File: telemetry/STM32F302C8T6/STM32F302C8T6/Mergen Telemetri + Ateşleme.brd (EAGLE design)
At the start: 49.7 x 87.5 mm, 91 parts, among them J2 U.FL, Q2 IRLML6344TRPBF, Q3 IRLML6344TRPBF, U2 BMP280, U3 MPU-6050, U4 L86, U6 AMS1117-3.3, U7 AMS1117-3.3, U8 STM32F302C8T6, X1 JST-XH-04-PIN-LONG-PAD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

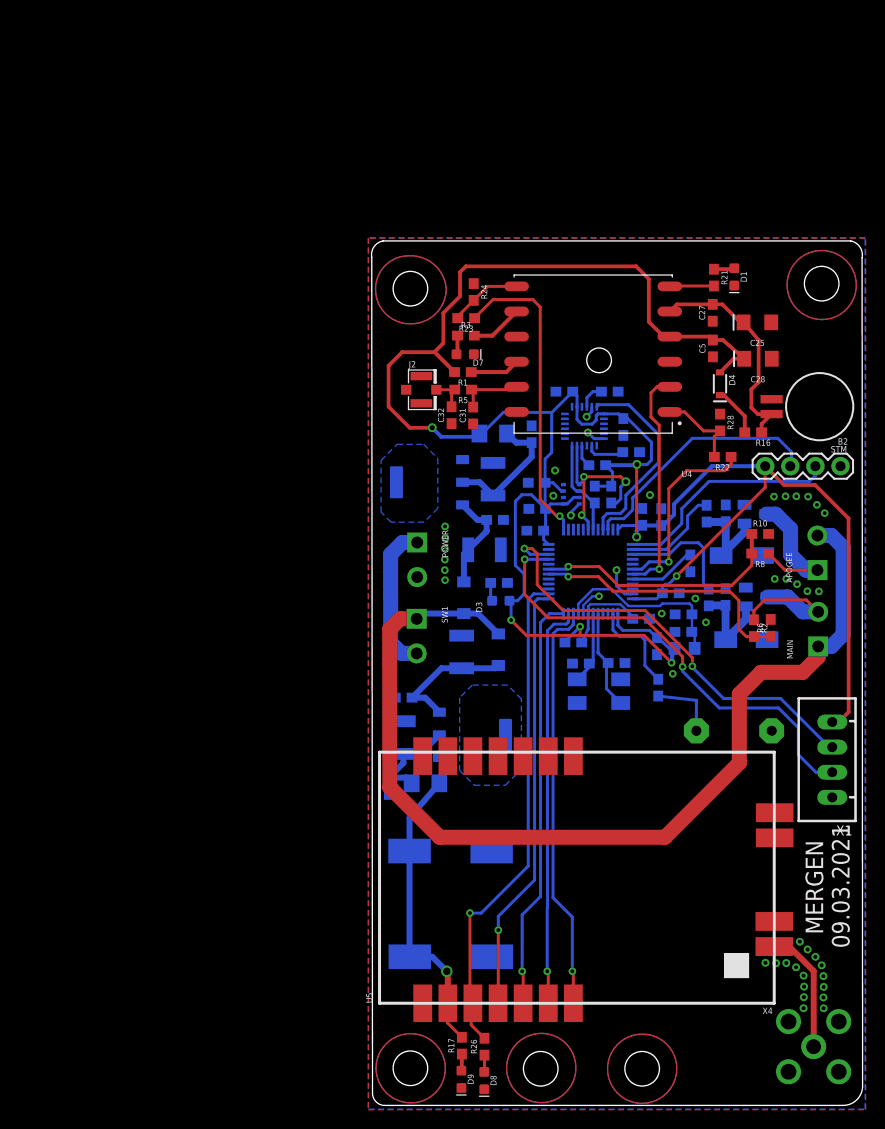
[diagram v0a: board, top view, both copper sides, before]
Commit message: Component name locations was arranged
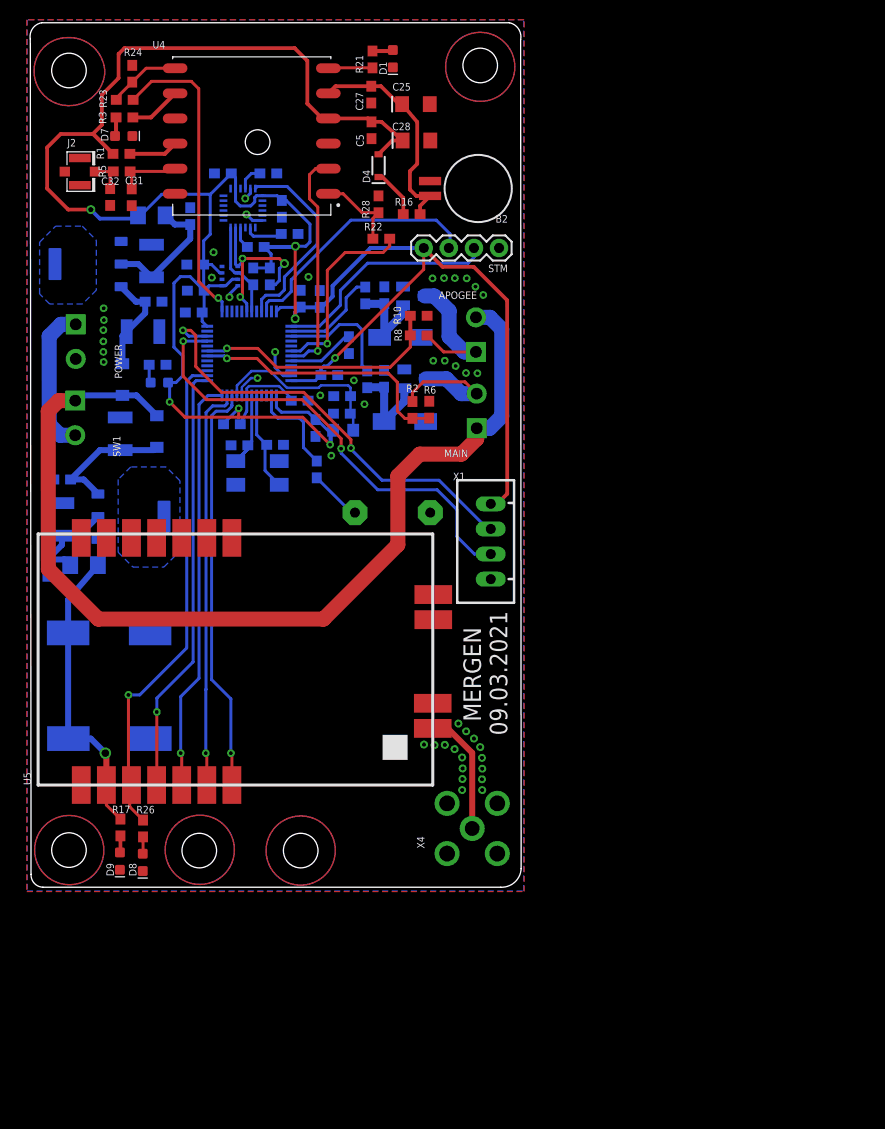
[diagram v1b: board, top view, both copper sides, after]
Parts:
- moved VDDA4 41.0 mm to (31.5, 48.0)
- moved C2 41.0 mm to (9.07, 45.9)
- moved C25 41.0 mm to (39.0, 79.3)
- moved C4 41.0 mm to (1.70, 32.4)
- moved C6 41.0 mm to (3.17, 37.3)
- moved C8 41.0 mm to (12.4, 59.3)
- moved D1 41.0 mm to (36.7, 83.9)
- moved D3 41.0 mm to (9.30, 51.4)
- moved D4 41.0 mm to (35.2, 73.1)
- moved ESDA 41.0 mm to (37.9, 47.2)
- moved ESDA1 41.0 mm to (37.4, 55.7)
- moved Q2 41.0 mm to (38.9, 51.5)
- moved Q3 41.0 mm to (38.8, 59.9)
- moved R16 41.0 mm to (38.6, 68.2)
- moved R2 41.0 mm to (38.6, 48.4)
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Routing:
- net N$8: track 6.97 -> 5.32 mm
